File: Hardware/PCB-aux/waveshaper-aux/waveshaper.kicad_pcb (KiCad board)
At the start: 2 copper layers, 189 x 174 mm, 59 parts, among them J1 2x7 IDC header, J10 AudioJack2_SwitchT, J11 3_pin_Molex_header, J12 AudioJack2_SwitchT, J13 2x5 pin socket, J14 AudioJack2_SwitchT, J15 AudioJack2_SwitchT, J16 AudioJack2_SwitchT, J17 AudioJack2_SwitchT, J2 AudioJack2_SwitchT, J3 AudioJack2_SwitchT, J4 2_pin_Molex_header, J5 EURO_PWR_2x5, J6 AudioJack2_SwitchT, J7 Conn_01x9, J8 2_pin_Molex_header, J9 Conn_01x9, SW1 SW_SPDT, U1 4066, U2 4066

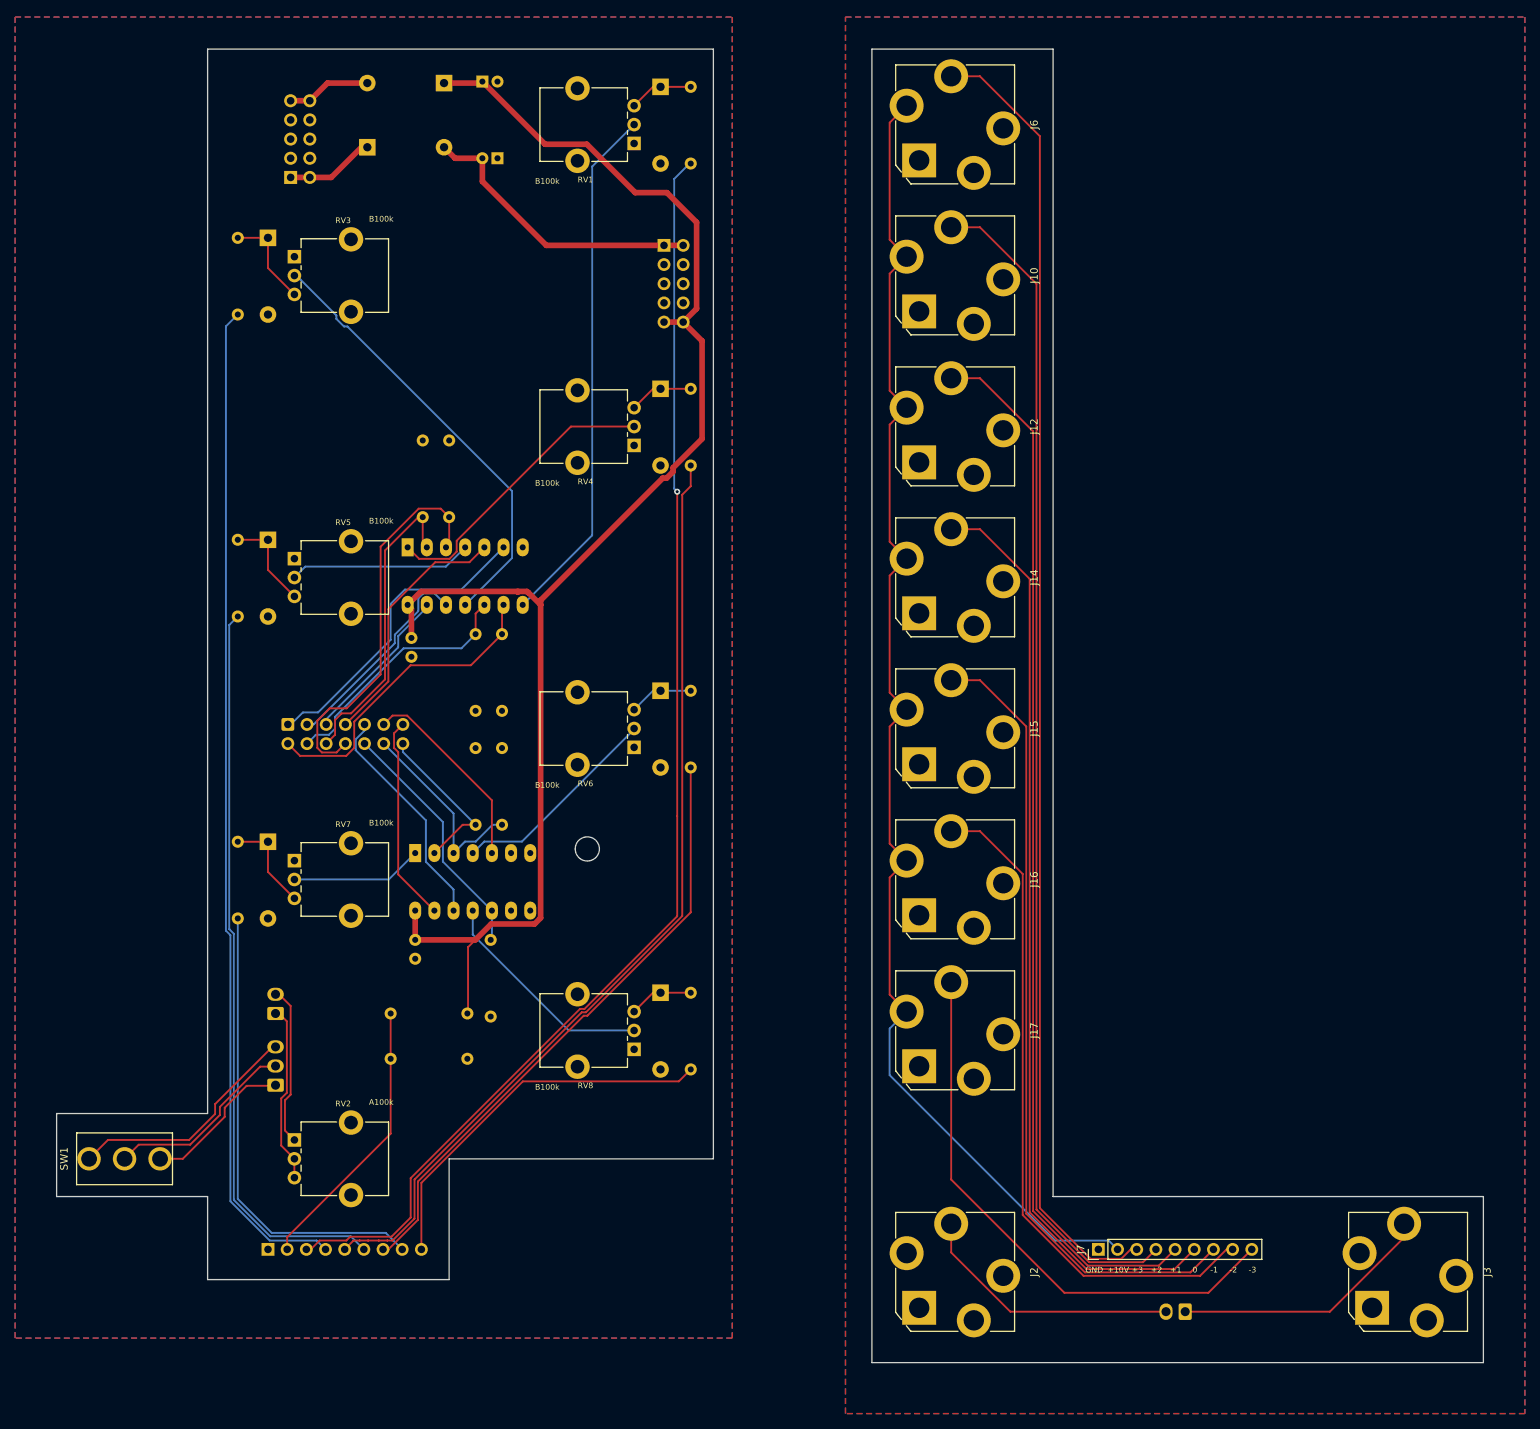
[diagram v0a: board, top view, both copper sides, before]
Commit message: Big redo: Add voltage ref, buffers; rm diodes
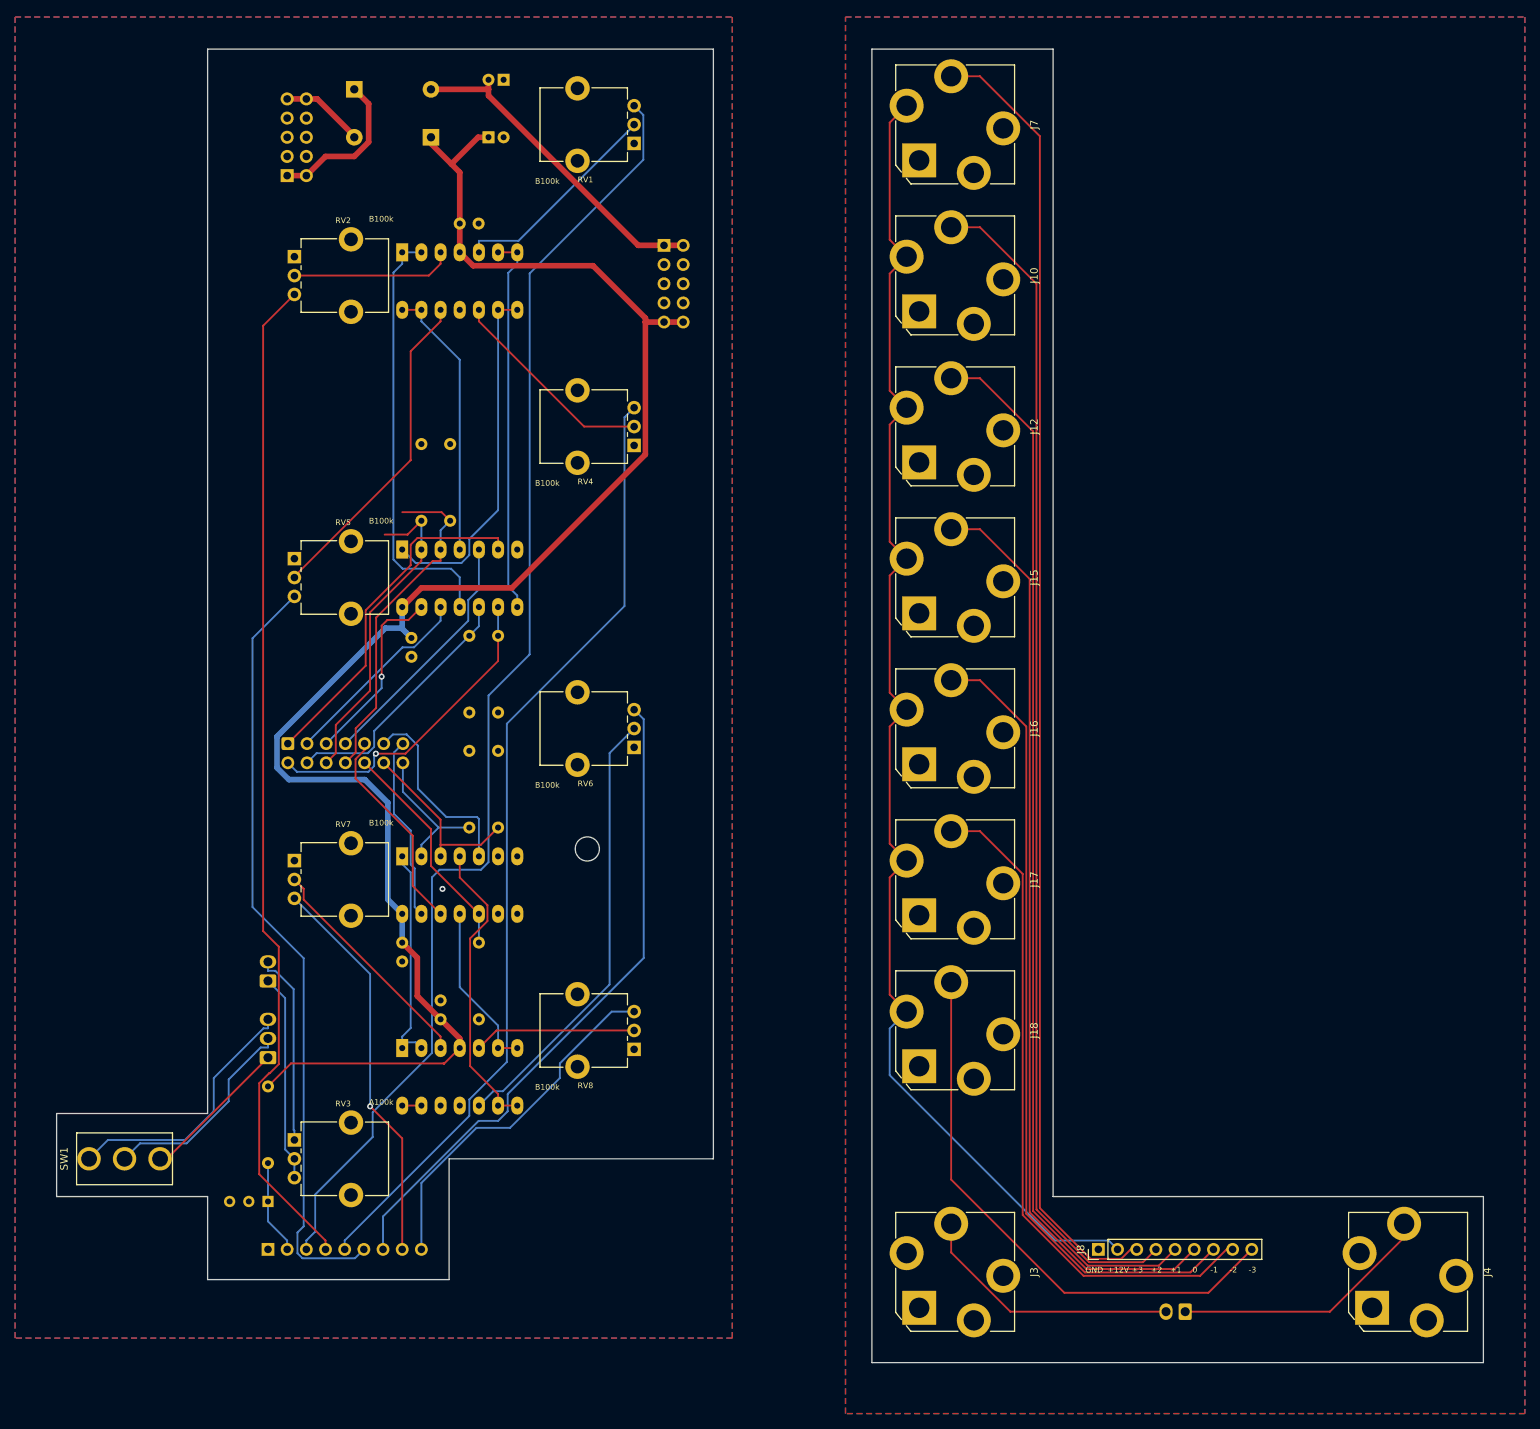
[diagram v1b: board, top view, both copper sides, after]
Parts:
- removed the D1 at (172.0, 24.0)
- removed the D2 at (120.0, 44.0)
- removed D5, D6, D7, D8, D9: 1N5817, ao_tht:D_DO-41_SOD81_P10.16mm_Horizontal
- removed R10, R11, R12, R13, R14, R15, R16: 1k, ao_tht:R_Axial_DIN0207_L6.3mm_D2.5mm_P10.16mm_Horizontal
- removed R9: 470k, ao_tht:R_Axial_DIN0207_L6.3mm_D2.5mm_P10.16mm_Horizontal
- added C1: 100nF, ao_tht:C_Disc_D3.0mm_W1.6mm_P2.50mm, B.Cu at (145.4, 42.1)
- added C2: 100nF, ao_tht:C_Disc_D3.0mm_W1.6mm_P2.50mm, B.Cu at (142.9, 147.5)
- added U3: MCP6004, ao_tht:DIP-14_W7.62mm_Socket_LongPads, B.Cu at (137.8, 45.9)
- added U4: MCP6004, ao_tht:DIP-14_W7.62mm_Socket_LongPads, B.Cu at (137.8, 151.3)
- added U5: LM4040DIZ-10, ao_tht:TO-92_Inline_Wide, B.Cu at (120.0, 171.7)
- C5: renamed from C3; value 0.1uF -> 100nF
- C6: renamed from C4; value 0.1uF -> 100nF
- R8: value 100k -> 1k
- moved GRAF1 46.6 mm to (168.9, 96.1), turned to 270 degrees
- moved R8 18.9 mm to (120.0, 156.4), turned to 270 degrees
- moved C4 10.4 mm to (151.2, 23.1)
- moved D2 7.86 mm to (131.4, 24.3)
- moved C3 7.42 mm to (149.2, 30.7)
- moved D1 7.39 mm to (141.6, 30.7)
- moved J11 4.42 mm to (120.0, 142.4)
- moved J13 3.78 mm to (120.0, 152.6)
- moved J1 2.54 mm to (122.6, 111.0)
- moved U2 1.77 mm to (137.8, 125.9)
- moved C6 1.76 mm to (137.8, 137.4)
- moved R4 1.60 mm to (147.9, 137.4)
- moved R7 0.91 mm to (146.7, 122.1)
- moved R5 0.86 mm to (146.7, 96.7)
- moved U1 0.78 mm to (137.8, 85.3)
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- renumbered C1 to C3, C2 to C4, D3 to D1, D4 to D2, J8 to J11, J11 to J13, J13 to J14, J14 to J15, J15 to J16, J16 to J17, J17 to J18, J2 to J3, J3 to J4, J4 to J5, J5 to J6, J6 to J7, J7 to J8, RV3 to RV2, RV2 to RV3
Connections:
- net Net-(D3-Pad2) renamed /Panel and power/+12V_IN
- net Net-(D4-Pad1) renamed /Panel and power/-12V_IN
- R8 pad 1: +10V -> +12V
- R8 pad 2: +12V -> +10V
- RV1 pad 2: CV_+3 -> P_+3
- RV1 pad 3: Net-(D1-Pad1) -> Net-(J9-Pad3)
- RV2 pad 2: CV_+2 -> P_+2
- RV2 pad 3: Net-(D2-Pad1) -> Net-(J9-Pad4)
- RV4 pad 2: CV_+1 -> P_+1
- RV4 pad 3: Net-(D5-Pad1) -> Net-(J9-Pad5)
- RV5 pad 2: CV_0 -> P_0
- RV5 pad 3: Net-(D6-Pad1) -> Net-(J9-Pad6)
- RV6 pad 2: CV_-1 -> P_-1
- RV6 pad 3: Net-(D7-Pad1) -> Net-(J9-Pad7)
- RV7 pad 2: CV_-2 -> P_-2
- RV7 pad 3: Net-(D8-Pad1) -> Net-(J9-Pad8)
- RV8 pad 2: CV_-3 -> P_-3
- RV8 pad 3: Net-(D9-Pad1) -> Net-(J9-Pad9)
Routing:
- net P_-1: track 0.00 -> 59.2 mm
- net P_0: track 0.00 -> 43.5 mm
- net P_-2: track 0.00 -> 30.3 mm
- net P_+3: track 0.00 -> 28.5 mm
- net P_+1: track 0.00 -> 27.9 mm
- net +12V: track 202.5 -> 227.3 mm
- net +10V: track 36.9 -> 12.5 mm
- net P_+2: track 0.00 -> 21.5 mm
- net P_-3: track 0.00 -> 21.5 mm
- net CV_+3: track 69.7 -> 50.5 mm
- net Net-(D8-Pad1): track 12.9 -> 0.00 mm
- net Net-(D6-Pad1): track 12.9 -> 0.00 mm
- net Net-(D2-Pad1): track 12.9 -> 0.00 mm
- net CV_0: track 24.3 -> 36.4 mm
- net CV_-2: track 17.4 -> 29.2 mm
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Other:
- net class Power added: clearance 0.2, trace_width 0.75, via_dia 0.8, via_drill 0.4
- board text removed: "+10V"

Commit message: Yes we need Schottkys
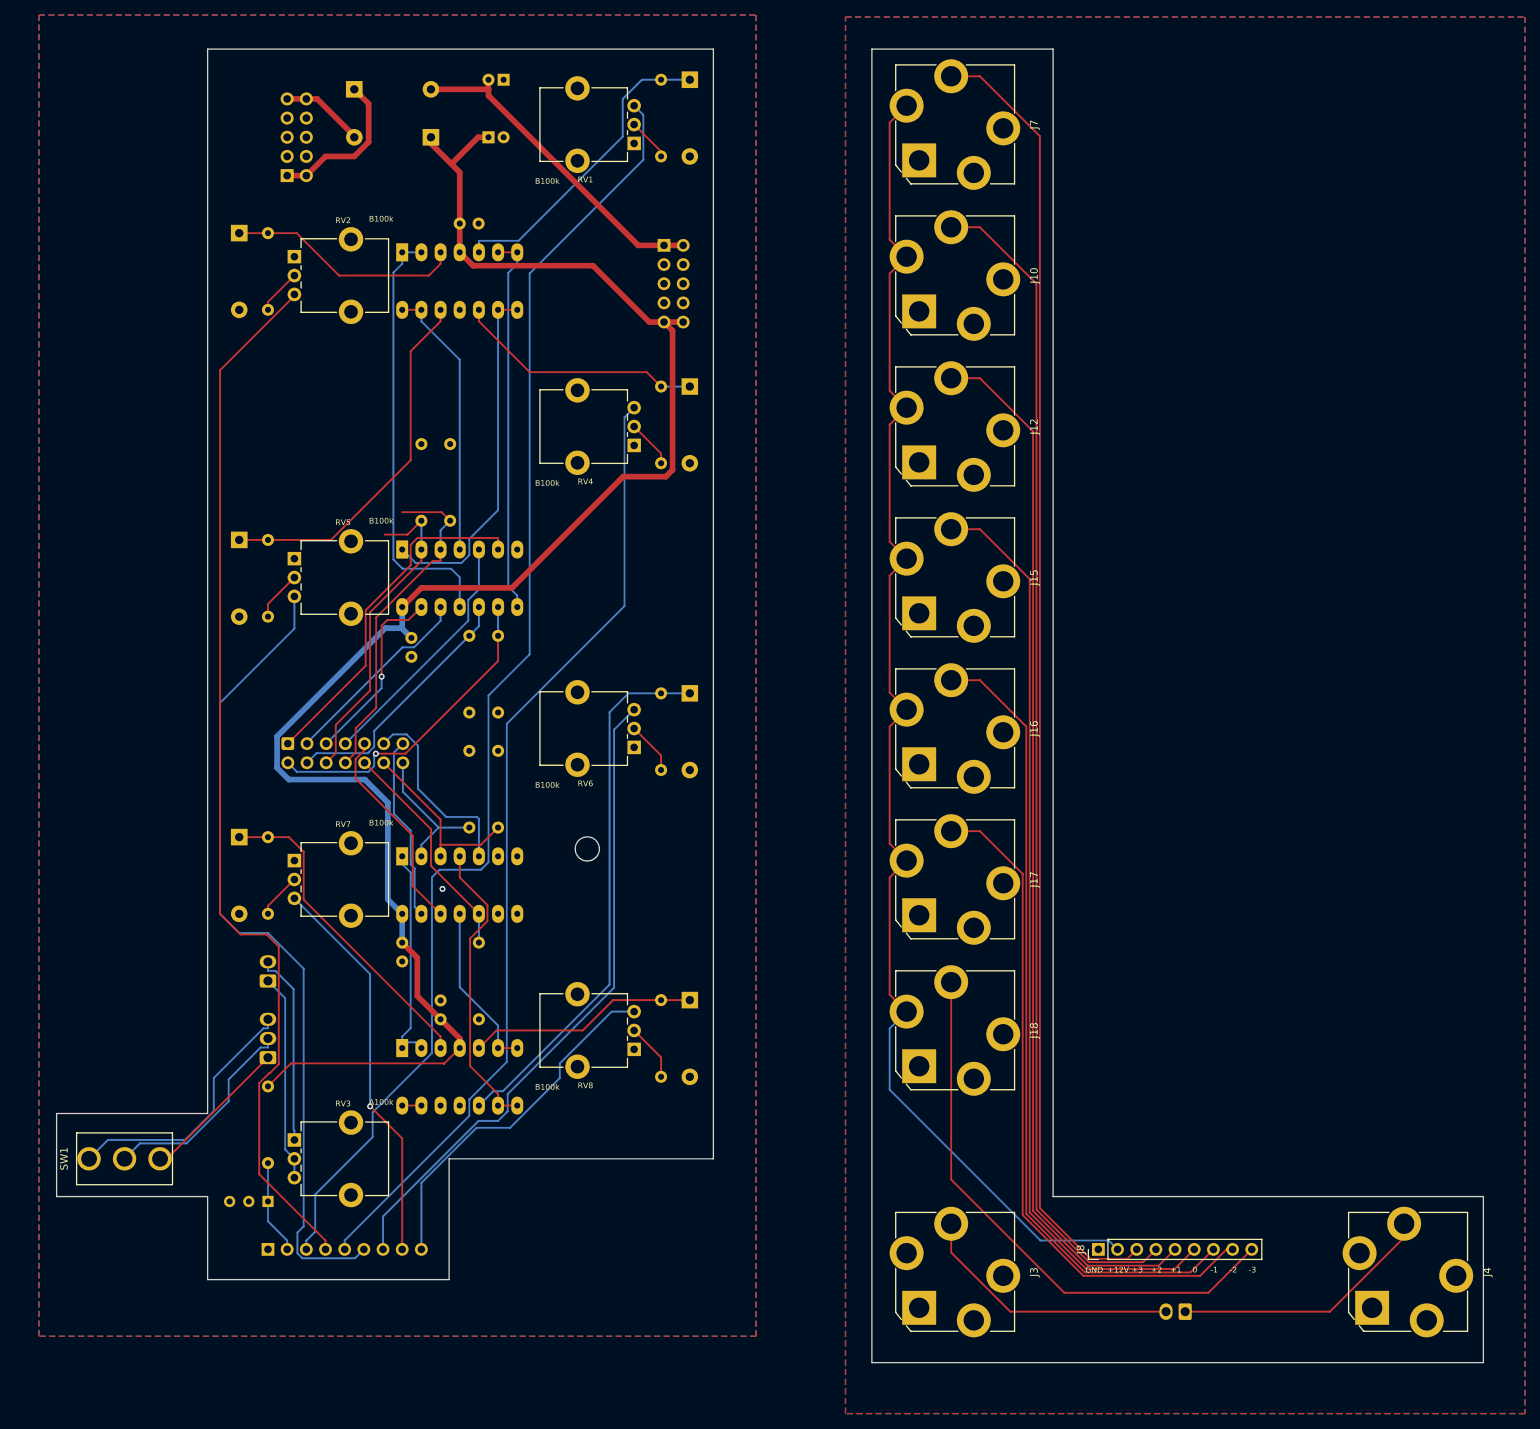
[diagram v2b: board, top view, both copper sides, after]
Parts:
- added D3: 1N5817, ao_tht:D_DO-41_SOD81_P10.16mm_Horizontal, B.Cu at (175.9, 23.1)
- added D4: 1N5817, ao_tht:D_DO-41_SOD81_P10.16mm_Horizontal, B.Cu at (116.2, 43.4)
- added D5: 1N5817, ao_tht:D_DO-41_SOD81_P10.16mm_Horizontal, B.Cu at (175.9, 63.7)
- added D6: 1N5817, ao_tht:D_DO-41_SOD81_P10.16mm_Horizontal, B.Cu at (116.2, 84.0)
- added D7: 1N5817, ao_tht:D_DO-41_SOD81_P10.16mm_Horizontal, B.Cu at (175.9, 104.3)
- added D8: 1N5817, ao_tht:D_DO-41_SOD81_P10.16mm_Horizontal, B.Cu at (116.2, 123.4)
- added D9: 1N5817, ao_tht:D_DO-41_SOD81_P10.16mm_Horizontal, B.Cu at (175.9, 145.0)
- added R10: 1k, ao_tht:R_Axial_DIN0207_L6.3mm_D2.5mm_P10.16mm_Horizontal, B.Cu at (120.0, 53.5)
- added R11: 1k, ao_tht:R_Axial_DIN0207_L6.3mm_D2.5mm_P10.16mm_Horizontal, B.Cu at (172.1, 73.9)
- added R12: 1k, ao_tht:R_Axial_DIN0207_L6.3mm_D2.5mm_P10.16mm_Horizontal, B.Cu at (120.0, 94.2)
- added R13: 1k, ao_tht:R_Axial_DIN0207_L6.3mm_D2.5mm_P10.16mm_Horizontal, B.Cu at (172.1, 114.5)
- added R14: 1k, ao_tht:R_Axial_DIN0207_L6.3mm_D2.5mm_P10.16mm_Horizontal, B.Cu at (120.0, 133.6)
- added R15: 1k, ao_tht:R_Axial_DIN0207_L6.3mm_D2.5mm_P10.16mm_Horizontal, B.Cu at (172.1, 155.1)
- added R9: 1k, ao_tht:R_Axial_DIN0207_L6.3mm_D2.5mm_P10.16mm_Horizontal, B.Cu at (172.1, 33.2)
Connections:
- RV1 pad 2: P_+3 -> Net-(R9-Pad1)
- RV2 pad 2: P_+2 -> Net-(R10-Pad1)
- RV4 pad 2: P_+1 -> Net-(R11-Pad1)
- RV5 pad 2: P_0 -> Net-(R12-Pad1)
- RV6 pad 2: P_-1 -> Net-(R13-Pad1)
- RV7 pad 2: P_-2 -> Net-(R14-Pad1)
- RV8 pad 2: P_-3 -> Net-(R15-Pad1)
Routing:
- net P_+3: track 28.5 -> 41.2 mm
- net P_-2: track 30.3 -> 42.8 mm
- net P_-1: track 59.2 -> 71.7 mm
- net P_+2: track 21.5 -> 31.2 mm
- net P_-3: track 21.5 -> 30.6 mm
- net Net-(R15-Pad1): track 0.00 -> 7.62 mm
- net Net-(R13-Pad1): track 0.00 -> 6.98 mm
- net Net-(R12-Pad1): track 0.00 -> 6.77 mm
- net Net-(J9-Pad4): track 133.8 -> 140.6 mm
- net Net-(R11-Pad1): track 0.00 -> 6.34 mm
- net Net-(R14-Pad1): track 0.00 -> 6.00 mm
- net Net-(R10-Pad1): track 0.00 -> 5.99 mm
- net Net-(J9-Pad6): track 102.0 -> 107.8 mm
- net Net-(R9-Pad1): track 0.00 -> 5.78 mm
- net P_+1: track 27.9 -> 33.0 mm
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
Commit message: Make pulldowns 100k
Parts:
- R1, R2, R3, R4, R5, R6, R7: value 10k -> 100k
